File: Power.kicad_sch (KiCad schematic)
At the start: 1 part

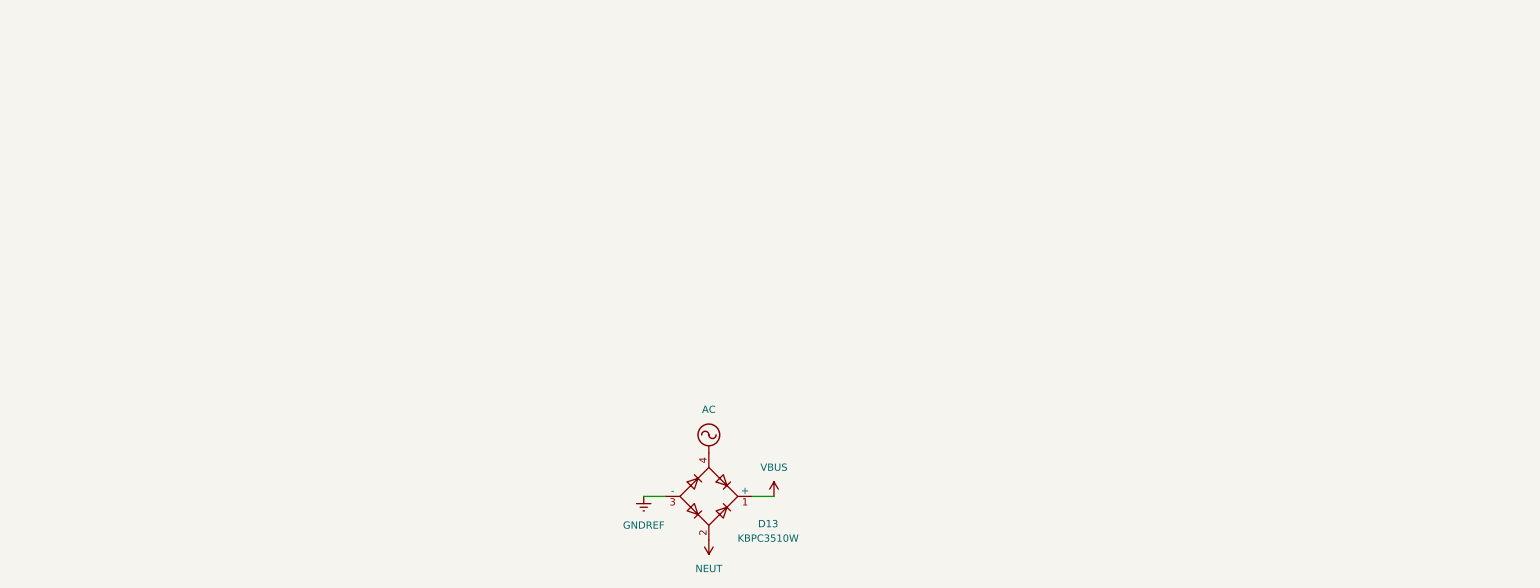
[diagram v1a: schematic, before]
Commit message: dev: added NC flags and fixed ERC warnings. Added custom design rules for PCB Design.
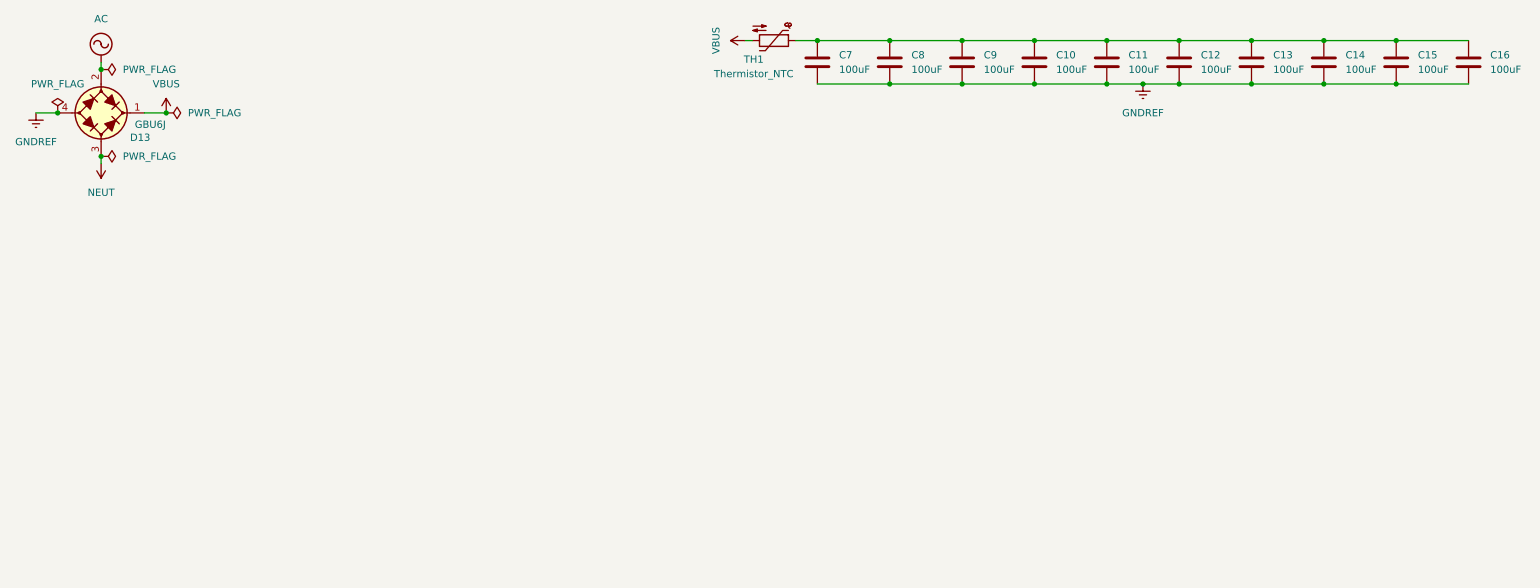
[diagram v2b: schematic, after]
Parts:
- removed D13: KBPC3510W, Diode_THT:Diode_Bridge_GeneSiC_KBPC_W, symbol Diode_Bridge:KBPC3510W
- added C10, C11, C12, C13, C14, C15, C16, C7, C8, C9: 100uF, Capacitor_THT:CP_Radial_D5.0mm_P2.00mm, symbol Device:C
- added D13: GBU6J, PCM_Diode_THT_AKL:Diode_Bridge_Vishay_GBU, symbol PCM_Diode_Bridge_AKL:GBU6J
- added TH1: Thermistor_NTC, Resistor_THT:R_Axial_DIN0204_L3.6mm_D1.6mm_P5.08mm_Vertical, symbol Device:Thermistor_NTC
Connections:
- net AC: now also D13.2 (1)
- net GNDREF: now also C10.2, C11.2, C12.2, C13.2, C14.2, C15.2, C16.2, C7.2, C8.2, C9.2, D13.4 (-)
- net NEUT: now also D13.3 (2)
- net VBUS: now also D13.1 (+), TH1.2
- new net: C10.1, C11.1, C12.1, C13.1, C14.1, C15.1, C16.1, C7.1, C8.1, C9.1, TH1.1
